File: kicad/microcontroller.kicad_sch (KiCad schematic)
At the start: 46 parts, among them J301 DEBUG_HEADER, Q301 2N7002, SW501 SW_Push_45deg, U301 RP2040, U302 W25Q128JVS, Y301 12MHz 20pF

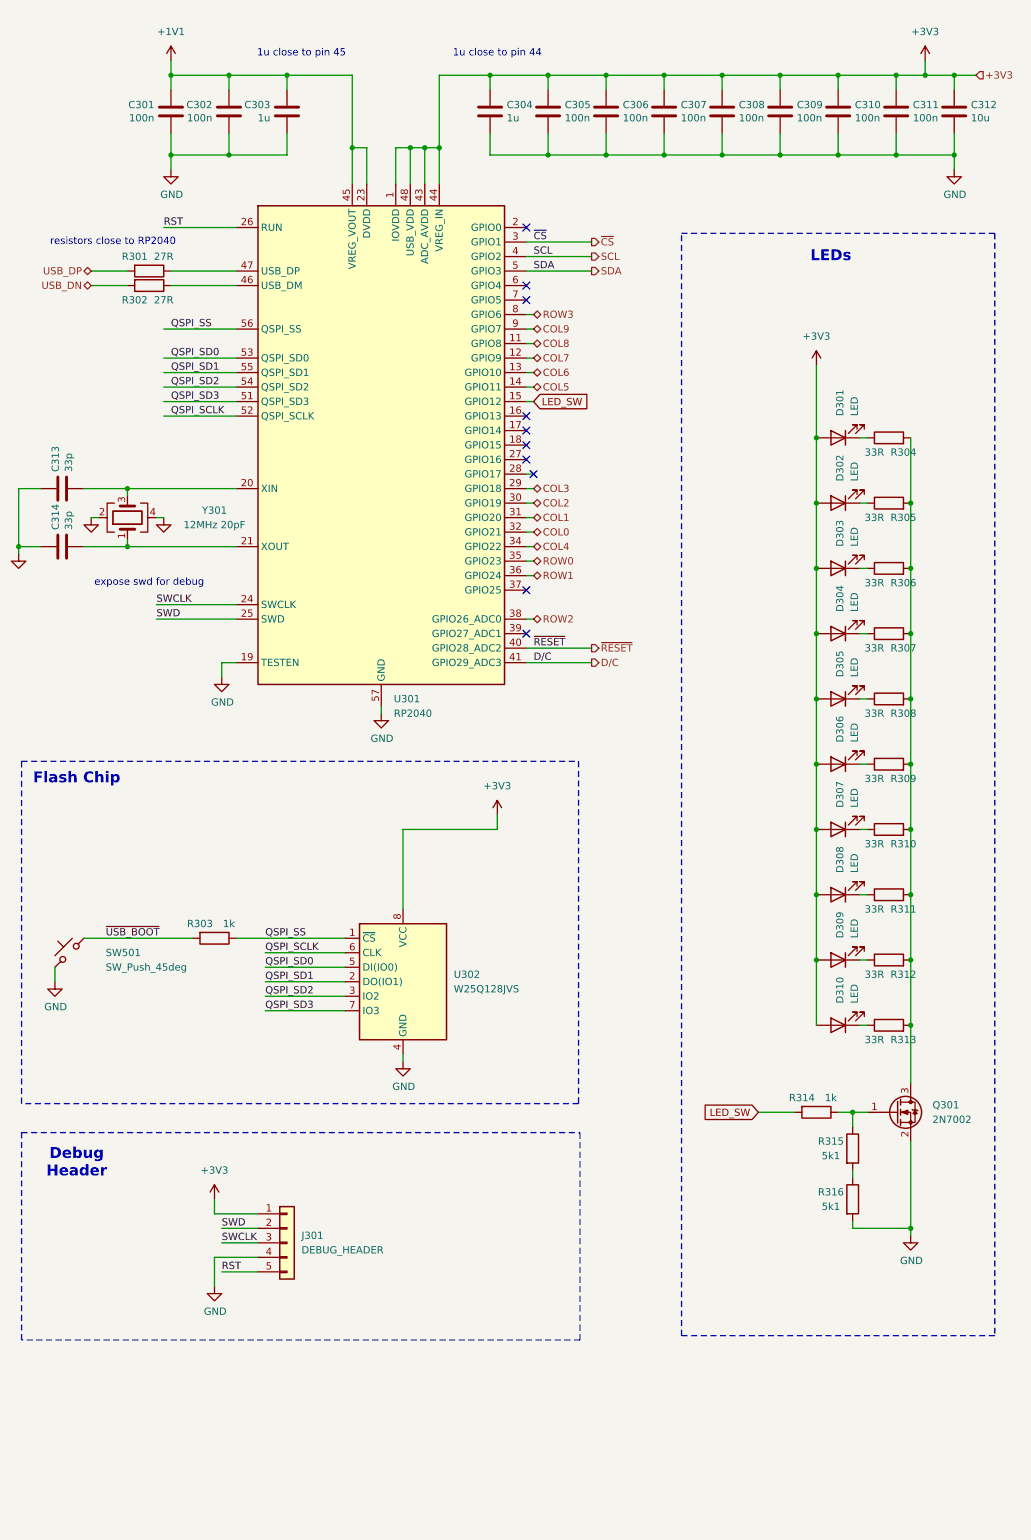
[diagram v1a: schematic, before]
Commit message: changed from rp2040 to nrf
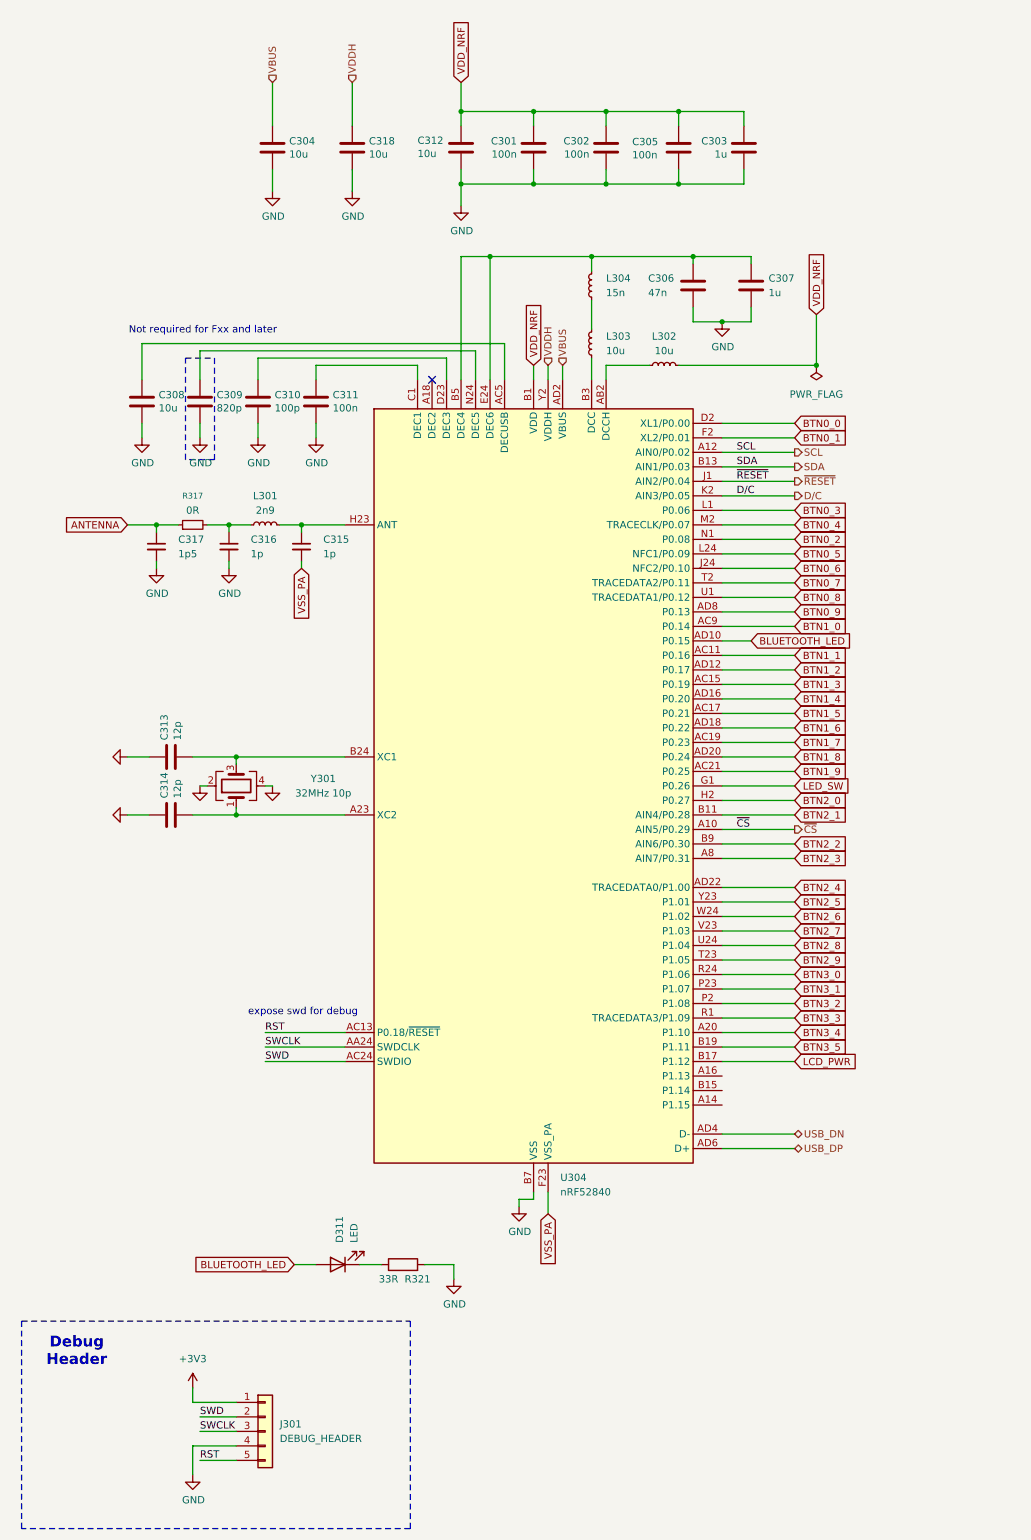
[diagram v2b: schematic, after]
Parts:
- removed D301, D302, D303, D304, D305, D306, D307, D308, D309, D310: LED, LED_SMD:LED_0603_1608Metric, symbol Device:LED
- removed Q301: 2N7002, Package_TO_SOT_SMD:SOT-23, symbol Transistor_FET:2N7002
- removed R301, R302: 27R, Resistor_SMD:R_0402_1005Metric, symbol Device:R
- removed R303, R314: 1k, Resistor_SMD:R_0402_1005Metric, symbol Device:R
- removed R304, R305, R306, R307, R308, R309, R310, R311, R312, R313: 33R, Resistor_SMD:R_0402_1005Metric, symbol Device:R
- removed R315, R316: 5k1, Resistor_SMD:R_0603_1608Metric, symbol Device:R
- removed SW501: SW_Push_45deg, Button_Switch_SMD:SW_Push_1P1T_XKB_TS-1187A, symbol Switch:SW_Push_45deg
- removed U301: RP2040, Package_DFN_QFN:QFN-56-1EP_7x7mm_P0.4mm_EP3.2x3.2mm, symbol MCU_RaspberryPi:RP2040
- removed U302: W25Q128JVS, Package_SO:SOIC-8_5.23x5.23mm_P1.27mm, symbol Memory_Flash:W25Q128JVS
- added C315, C316: 1p, Capacitor_SMD:C_0402_1005Metric, symbol Device:C_Small
- added C317: 1p5, Capacitor_SMD:C_0402_1005Metric, symbol Device:C_Small
- added C318: 10u, Capacitor_SMD:C_0402_1005Metric, symbol Device:C
- added D311: LED, LED_SMD:LED_0603_1608Metric, symbol Device:LED
- added L301: 2n9, Inductor_SMD:L_0402_1005Metric, symbol Device:L_Small
- added L302, L303: 10u, Inductor_SMD:L_APV_ANR252012, symbol Device:L_Small
- added L304: 15n, Inductor_SMD:L_0603_1608Metric, symbol Device:L_Small
- added R317: 0R, Resistor_SMD:R_0402_1005Metric, symbol Device:R_Small
- added R321: 33R, Resistor_SMD:R_0402_1005Metric, symbol Device:R
- added U304: nRF52840, Package_DFN_QFN:Nordic_AQFN-73-1EP_7x7mm_P0.5mm, symbol MCU_Nordic:nRF52840
- C304: value 1u -> 10u; JLCPCB Part # C52923 -> C15525
- C306: value 100n -> 47n; JLCPCB Part # C1525 -> C82219
- C307: value 100n -> 1u; JLCPCB Part # C1525 -> C52923
- C308: value 100n -> 10u; JLCPCB Part # C1525 -> C15525
- C309: value 100n -> 820p; JLCPCB Part # C1525 -> C1543
- C310: value 100n -> 100p; JLCPCB Part # C1525 -> C1546
- C312: footprint Capacitor_SMD:C_0603_1608Metric -> Capacitor_SMD:C_0402_1005Metric; JLCPCB Part # C19702 -> C15525
- C313, C314: value 33p -> 12p; JLCPCB Part # C1562 -> C1547
- Y301: value 12MHz 20pF -> 32MHz 10p; JLCPCB Part # C9002 -> C113671
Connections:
- net +3V3: no longer C304.1, C305.1, C306.1, C307.1, C308.1, C309.1, C310.1, C311.1, C312.1
- net D/C: now also U304.K2 (AIN3/P0.05)
- net GND: now also C316.2, C317.2, C318.2, R321.2, U304.B7 (VSS), U304.EP (VSS)
- net LED_SW: now also U304.G1 (P0.26)
- net RST: now also U304.AC13 (P0.18/~{RESET})
- net SCL: now also U304.A12 (AIN0/P0.02)
- net SDA: now also U304.B13 (AIN1/P0.03)
- net SWCLK: now also U304.AA24 (SWDCLK)
- net SWD: now also U304.AC24 (SWDIO)
- net USB_DN: now also U304.AD4 (D-)
- net USB_DP: now also U304.AD6 (D+)
- net ~{CS}: now also U304.A10 (AIN5/P0.29)
- net ~{RESET}: now also U304.J1 (AIN2/P0.04)
- net at C313.2, Y301.3: now also U304.B24 (XC1)
- net at C314.2, Y301.1: now also U304.A23 (XC2)
- net +1V1 renamed VDD_NRF
- net VDD_NRF: now also C305.1, C312.1, L302.2, U304.A22 (VDD), U304.AD14 (VDD), U304.AD23 (VDD), U304.B1 (VDD), U304.W1 (VDD)
- new net: C309.1, U304.N24 (DEC5)
- new net: C315.1, L301.2, U304.H23 (ANT)
- new net: L302.1, U304.AB2 (DCCH)
- new net: C308.1, U304.AC5 (DECUSB)
- new net: L303.1, U304.B3 (DCC)
- new net: C306.1, C307.1, L304.2, U304.B5 (DEC4), U304.E24 (DEC6)
- new net: C311.1, U304.C1 (DEC1)
- new net: C310.1, U304.D23 (DEC3)
- new net: D311.1 (K), R321.1
- new net: L303.2, L304.1
- new net: C316.1, L301.1, R317.2
- new net ANTENNA: C317.1, R317.1
- new net BLUETOOTH_LED: D311.2 (A), U304.AD10 (P0.15)
- new net BTN0_0: U304.D2 (XL1/P0.00)
- new net BTN0_1: U304.F2 (XL2/P0.01)
- new net BTN0_2: U304.N1 (P0.08)
- new net BTN0_3: U304.L1 (P0.06)
- new net BTN0_4: U304.M2 (TRACECLK/P0.07)
- new net BTN0_5: U304.L24 (NFC1/P0.09)
- new net BTN0_6: U304.J24 (NFC2/P0.10)
- new net BTN0_7: U304.T2 (TRACEDATA2/P0.11)
- new net BTN0_8: U304.U1 (TRACEDATA1/P0.12)
- new net BTN0_9: U304.AD8 (P0.13)
- new net BTN1_0: U304.AC9 (P0.14)
- new net BTN1_1: U304.AC11 (P0.16)
- new net BTN1_2: U304.AD12 (P0.17)
- new net BTN1_3: U304.AC15 (P0.19)
- new net BTN1_4: U304.AD16 (P0.20)
- new net BTN1_5: U304.AC17 (P0.21)
- new net BTN1_6: U304.AD18 (P0.22)
- new net BTN1_7: U304.AC19 (P0.23)
- new net BTN1_8: U304.AD20 (P0.24)
- new net BTN1_9: U304.AC21 (P0.25)
- new net BTN2_0: U304.H2 (P0.27)
- new net BTN2_1: U304.B11 (AIN4/P0.28)
- new net BTN2_2: U304.B9 (AIN6/P0.30)
- new net BTN2_3: U304.A8 (AIN7/P0.31)
- new net BTN2_4: U304.AD22 (TRACEDATA0/P1.00)
- new net BTN2_5: U304.Y23 (P1.01)
- new net BTN2_6: U304.W24 (P1.02)
- new net BTN2_7: U304.V23 (P1.03)
- new net BTN2_8: U304.U24 (P1.04)
- new net BTN2_9: U304.T23 (P1.05)
- new net BTN3_0: U304.R24 (P1.06)
- new net BTN3_1: U304.P23 (P1.07)
- new net BTN3_2: U304.P2 (P1.08)
- new net BTN3_3: U304.R1 (TRACEDATA3/P1.09)
- new net BTN3_4: U304.A20 (P1.10)
- new net BTN3_5: U304.B19 (P1.11)
- new net LCD_PWR: U304.B17 (P1.12)
- new net VBUS: C304.1, U304.AD2 (VBUS)
- new net VDDH: C318.1, U304.Y2 (VDDH)
- new net VSS_PA: C315.2, U304.F23 (VSS_PA)
- no-connect marks 10 -> 1
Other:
- note added: "Not required for Fxx and later"
- note removed: "1u close to pin 44"
- note removed: "1u close to pin 45"
- note removed: "Flash Chip"
- note removed: "LEDs"
- note removed: "resistors close to RP2040"
- moved on the sheet: C301, C302, C303, C304, C305, C306, C307, C308, C309, C310, C311, C312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

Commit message: board routed
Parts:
- added AE301: Antenna, mikoto:2.4GHz-meander-antenna-v2-inverted, symbol Device:Antenna
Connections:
- net +3V3 is gone; now on net VDD_NRF: J301.1 (Pin_1)
- net D/C: now also U304.A14 (P1.15); no longer U304.K2 (AIN3/P0.05)
- net ~{CS}: now also U304.A16 (P1.13); no longer U304.A10 (AIN5/P0.29)
- net ~{RESET}: now also U304.B15 (P1.14); no longer U304.J1 (AIN2/P0.04)
- net ANTENNA: no longer names the net of C317.1, R317.1
- net ANTENNA: now also AE301.1 (A)
- net BTN0_0: no longer names the net of U304.D2 (XL1/P0.00)
- net BTN0_1: no longer names the net of U304.F2 (XL2/P0.01)
- net BTN0_2 renamed COL7
- net BTN0_3 renamed COL8
- net BTN0_4 renamed BAT_I2C_SCL
- net BTN0_5 renamed COL0
- net BTN0_6: no longer names the net of U304.J24 (NFC2/P0.10)
- net BTN0_7 renamed BAT_I2C_SDA
- net BTN0_8 renamed COL5
- net BTN0_9: no longer names the net of U304.AD8 (P0.13)
- net BTN1_0: no longer names the net of U304.AC9 (P0.14)
- net BTN1_1: no longer names the net of U304.AC11 (P0.16)
- net BTN1_2: no longer names the net of U304.AD12 (P0.17)
- net BTN1_3: no longer names the net of U304.AC15 (P0.19)
- net BTN1_4: no longer names the net of U304.AD16 (P0.20)
- net BTN1_5: no longer names the net of U304.AC17 (P0.21)
- net BTN1_6: no longer names the net of U304.AD18 (P0.22)
- net BTN1_7: no longer names the net of U304.AC19 (P0.23)
- net BTN1_8: no longer names the net of U304.AD20 (P0.24)
- net BTN1_9: no longer names the net of U304.AC21 (P0.25)
- net BTN2_0: no longer names the net of U304.H2 (P0.27)
- net BTN2_1 renamed ROW3
- net BTN2_2: no longer names the net of U304.B9 (AIN6/P0.30)
- net BTN2_3: no longer names the net of U304.A8 (AIN7/P0.31)
- net BTN2_4: no longer names the net of U304.AD22 (TRACEDATA0/P1.00)
- net BTN2_5 renamed ROW0
- net BTN2_6 renamed COL4
- net BTN2_7: no longer names the net of U304.V23 (P1.03)
- net BTN2_8 renamed COL3
- net BTN2_9: no longer names the net of U304.T23 (P1.05)
- net BTN3_0 renamed COL2
- net BTN3_1 renamed COL1
- net BTN3_2: no longer names the net of U304.P2 (P1.08)
- net BTN3_3 renamed COL6
- net BTN3_4: no longer names the net of U304.A20 (P1.10)
- net BTN3_5 renamed ROW1
- net LCD_PWR renamed ROW2
- net LED_SW renamed COL9
- new net P_BTN: U304.J1 (AIN2/P0.04)
- no-connect marks 1 -> 25
